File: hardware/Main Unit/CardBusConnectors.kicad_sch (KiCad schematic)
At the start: 5 parts, among them J2 61801525123, J3 61801525123, U3 SN74CB3Q3257PWR

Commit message: Finish 3.3V regulator
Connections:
- net V_SUPPLY renamed V_{SUPPLY}
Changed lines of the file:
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@@
 		)
 	)
-	(label "V_SUPPLY"
+	(label "V_{SUPPLY}"
 		(at 200.66 115.57 0)
 		(effects
@@
 		)
 	)
-	(label "V_SUPPLY"
+	(label "V_{SUPPLY}"
 		(at 203.2 48.26 0)
 		(effects
@@
 		)
 	)
-	(hierarchical_label "V_SUPPLY"
+	(hierarchical_label "V_{SUPPLY}"
 		(shape input)
 		(at 200.66 48.26 180)

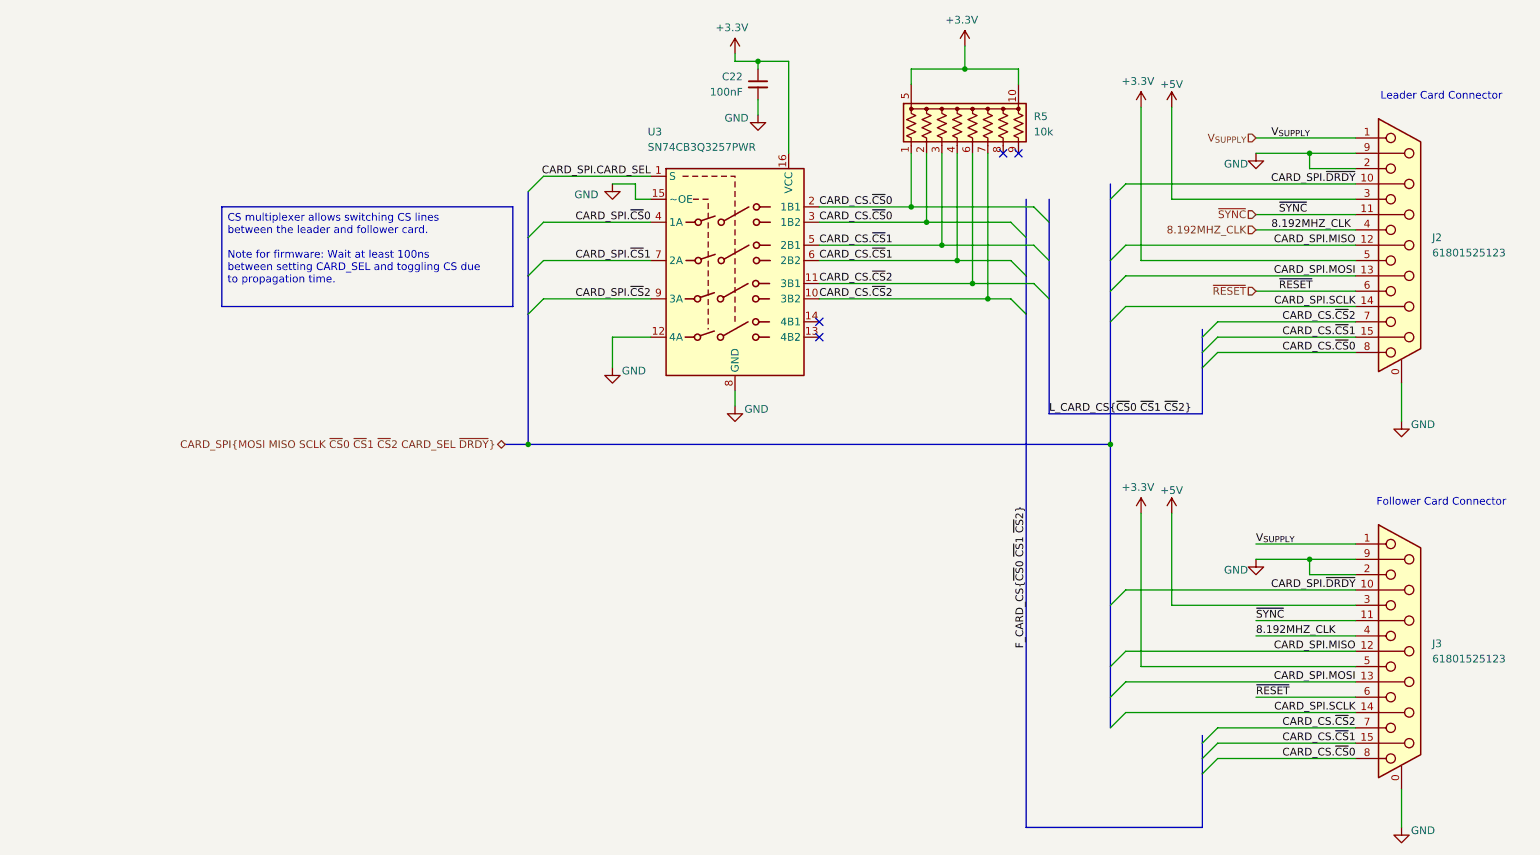
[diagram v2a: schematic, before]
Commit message: Main unit: Add USB port for MCU and 3.3VA rail, start on routing
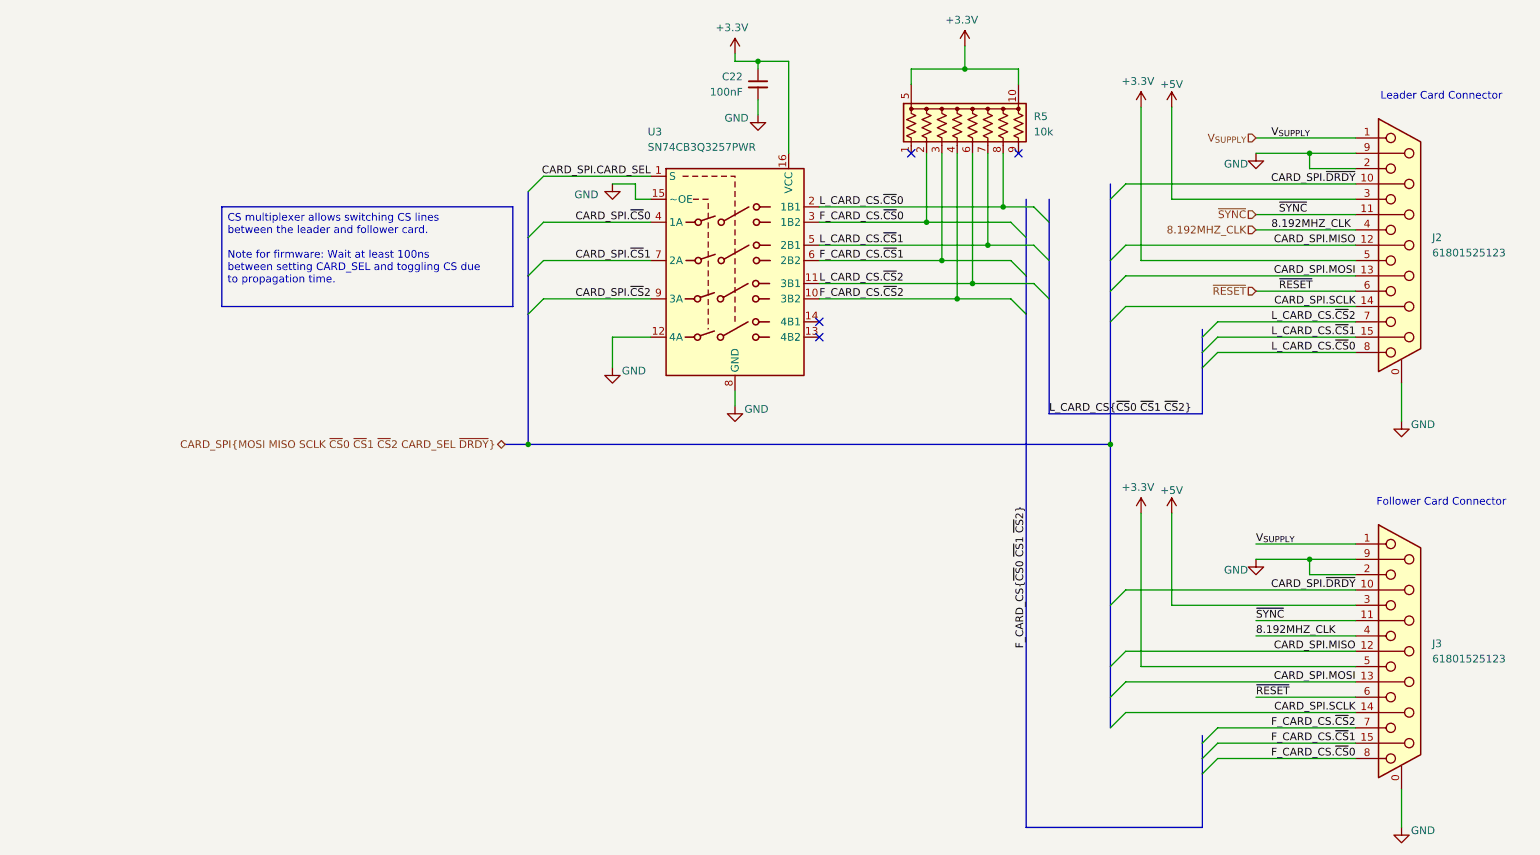
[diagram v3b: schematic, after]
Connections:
- net L_CARD_CS.~{CS}0: now reaches R5.8 (R7)
- net L_CARD_CS.~{CS}0: now also J2.8, U3.2 (1B1)
- net CARD_CS.~{CS}0 renamed F_CARD_CS.~{CS}0
- net F_CARD_CS.~{CS}0: no longer J2.8, R5.1 (R1), U3.2 (1B1)
- net CARD_CS.~{CS}1 renamed F_CARD_CS.~{CS}1
- net F_CARD_CS.~{CS}1: no longer J2.15 (P15), R5.4 (R4), U3.5 (2B1)
- net CARD_CS.~{CS}2 renamed L_CARD_CS.~{CS}2
- net L_CARD_CS.~{CS}2: no longer J3.7, R5.7 (R6), U3.10 (3B2)
- new net F_CARD_CS.~{CS}2: J3.7, R5.4 (R4), U3.10 (3B2)
- new net L_CARD_CS.~{CS}1: J2.15 (P15), R5.7 (R6), U3.5 (2B1)

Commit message: Geographical reannotate
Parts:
- renumbered C22 to C36, J3 to J6, J2 to J7, R5 to R12, U3 to U6
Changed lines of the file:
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@@
 		(dnp no)
 		(fields_autoplaced yes)
-		(property "Reference" "J3"
+		(property "Reference" "J6"
 			(at 229.87 132.0799 0)
 			(effects
@@
 			(project "HackerDAQ Main Unit"
 				(path "/7d91f165-331a-4c48-9d02-ee2a0aa7e94a/647fa122-ba55-4257-82a5-33756e3f8461"
-					(reference "J3")
-					(unit 1)
-				)
-				(path "/7d91f165-331a-4c48-9d02-ee2a0aa7e94a/65abad2d-a04a-4486-8762-5ae3bd8749b5"
-					(reference "J9")
-					(unit 1)
-				)
-				(path "/7d91f165-331a-4c48-9d02-ee2a0aa7e94a/9f275358-f91d-4a0c-a7c6-dd286f9a4cb9"
-					(reference "J7")
-					(unit 1)
-				)
-				(path "/7d91f165-331a-4c48-9d02-ee2a0aa7e94a/a26c9c83-f4f8-48b6-a052-d2759c00eb1e"
-					(reference "J5")
+					(reference "J6")
+					(unit 1)
+				)
+				(path "/7d91f165-331a-4c48-9d02-ee2a0aa7e94a/65abad2d-a04a-4486-8762-5ae3bd8749b5"
+					(reference "J2")
+					(unit 1)
+				)
+				(path "/7d91f165-331a-4c48-9d02-ee2a0aa7e94a/9f275358-f91d-4a0c-a7c6-dd286f9a4cb9"
+					(reference "J4")
+					(unit 1)
+				)
+				(path "/7d91f165-331a-4c48-9d02-ee2a0aa7e94a/a26c9c83-f4f8-48b6-a052-d2759c00eb1e"
+					(reference "J8")
 					(unit 1)
 				)
@@
 		(dnp no)
 		(fields_autoplaced yes)
-		(property "Reference" "J2"
+		(property "Reference" "J7"
 			(at 229.87 64.7699 0)
 			(effects
@@
 			(project "HackerDAQ Main Unit"
 				(path "/7d91f165-331a-4c48-9d02-ee2a0aa7e94a/647fa122-ba55-4257-82a5-33756e3f8461"
-					(reference "J2")
-					(unit 1)
-				)
-				(path "/7d91f165-331a-4c48-9d02-ee2a0aa7e94a/65abad2d-a04a-4486-8762-5ae3bd8749b5"
-					(reference "J8")
-					(unit 1)
-				)
-				(path "/7d91f165-331a-4c48-9d02-ee2a0aa7e94a/9f275358-f91d-4a0c-a7c6-dd286f9a4cb9"
-					(reference "J6")
-					(unit 1)
-				)
-				(path "/7d91f165-331a-4c48-9d02-ee2a0aa7e94a/a26c9c83-f4f8-48b6-a052-d2759c00eb1e"
-					(reference "J4")
+					(reference "J7")
+					(unit 1)
+				)
+				(path "/7d91f165-331a-4c48-9d02-ee2a0aa7e94a/65abad2d-a04a-4486-8762-5ae3bd8749b5"
+					(reference "J3")
+					(unit 1)
+				)
+				(path "/7d91f165-331a-4c48-9d02-ee2a0aa7e94a/9f275358-f91d-4a0c-a7c6-dd286f9a4cb9"
+					(reference "J5")
+					(unit 1)
+				)
+				(path "/7d91f165-331a-4c48-9d02-ee2a0aa7e94a/a26c9c83-f4f8-48b6-a052-d2759c00eb1e"
+					(reference "J9")
 					(unit 1)
 				)
@@
 		(dnp no)
 		(fields_autoplaced yes)
-		(property "Reference" "R5"
+		(property "Reference" "R12"
 			(at 163.83 44.7039 0)
 			(effects
@@
 			(project "HackerDAQ Main Unit"
 				(path "/7d91f165-331a-4c48-9d02-ee2a0aa7e94a/647fa122-ba55-4257-82a5-33756e3f8461"
-					(reference "R5")
-					(unit 1)
-				)
-				(path "/7d91f165-331a-4c48-9d02-ee2a0aa7e94a/65abad2d-a04a-4486-8762-5ae3bd8749b5"
-					(reference "R8")
-					(unit 1)
-				)
-				(path "/7d91f165-331a-4c48-9d02-ee2a0aa7e94a/9f275358-f91d-4a0c-a7c6-dd286f9a4cb9"
-					(reference "R7")
-					(unit 1)
-				)
-				(path "/7d91f165-331a-4c48-9d02-ee2a0aa7e94a/a26c9c83-f4f8-48b6-a052-d2759c00eb1e"
-					(reference "R6")
+					(reference "R12")
+					(unit 1)
+				)
+				(path "/7d91f165-331a-4c48-9d02-ee2a0aa7e94a/65abad2d-a04a-4486-8762-5ae3bd8749b5"
+					(reference "R11")
+					(unit 1)
+				)
+				(path "/7d91f165-331a-4c48-9d02-ee2a0aa7e94a/9f275358-f91d-4a0c-a7c6-dd286f9a4cb9"
+					(reference "R13")
+					(unit 1)
+				)
+				(path "/7d91f165-331a-4c48-9d02-ee2a0aa7e94a/a26c9c83-f4f8-48b6-a052-d2759c00eb1e"
+					(reference "R10")
 					(unit 1)
 				)
@@
 		(on_board yes)
 		(dnp no)
-		(property "Reference" "U3"
+		(property "Reference" "U6"
 			(at 99.822 47.244 0)
 			(effects
@@
 			(project "HackerDAQ Main Unit"
 				(path "/7d91f165-331a-4c48-9d02-ee2a0aa7e94a/647fa122-ba55-4257-82a5-33756e3f8461"
+					(reference "U6")
+					(unit 1)
+				)
+				(path "/7d91f165-331a-4c48-9d02-ee2a0aa7e94a/65abad2d-a04a-4486-8762-5ae3bd8749b5"
+					(reference "U7")
+					(unit 1)
+				)
+				(path "/7d91f165-331a-4c48-9d02-ee2a0aa7e94a/9f275358-f91d-4a0c-a7c6-dd286f9a4cb9"
+					(reference "U1")
+					(unit 1)
+				)
+				(path "/7d91f165-331a-4c48-9d02-ee2a0aa7e94a/a26c9c83-f4f8-48b6-a052-d2759c00eb1e"
 					(reference "U3")
-					(unit 1)
-				)
-				(path "/7d91f165-331a-4c48-9d02-ee2a0aa7e94a/65abad2d-a04a-4486-8762-5ae3bd8749b5"
-					(reference "U6")
-					(unit 1)
-				)
-				(path "/7d91f165-331a-4c48-9d02-ee2a0aa7e94a/9f275358-f91d-4a0c-a7c6-dd286f9a4cb9"
-					(reference "U5")
-					(unit 1)
-				)
-				(path "/7d91f165-331a-4c48-9d02-ee2a0aa7e94a/a26c9c83-f4f8-48b6-a052-d2759c00eb1e"
-					(reference "U4")
 					(unit 1)
 				)
@@
 		(on_board yes)
 		(dnp no)
-		(property "Reference" "C22"
+		(property "Reference" "C36"
 			(at 115.57 38.1062 0)
 			(effects
@@
 			(project "HackerDAQ Main Unit"
 				(path "/7d91f165-331a-4c48-9d02-ee2a0aa7e94a/647fa122-ba55-4257-82a5-33756e3f8461"
-					(reference "C22")
-					(unit 1)
-				)
-				(path "/7d91f165-331a-4c48-9d02-ee2a0aa7e94a/65abad2d-a04a-4486-8762-5ae3bd8749b5"
-					(reference "C26")
-					(unit 1)
-				)
-				(path "/7d91f165-331a-4c48-9d02-ee2a0aa7e94a/9f275358-f91d-4a0c-a7c6-dd286f9a4cb9"
-					(reference "C25")
-					(unit 1)
-				)
-				(path "/7d91f165-331a-4c48-9d02-ee2a0aa7e94a/a26c9c83-f4f8-48b6-a052-d2759c00eb1e"
-					(reference "C23")
-					(unit 1)
-				)
+					(reference "C36")
+					(unit 1)
+				)
+				(path "/7d91f165-331a-4c48-9d02-ee2a0aa7e94a/65abad2d-a04a-4486-8762-5ae3bd8749b5"
+					(reference "C28")
+					(unit 1)
+				)
+				(path "/7d91f165-331a-4c48-9d02-ee2a0aa7e94a/9f275358-f91d-4a0c-a7c6-dd286f9a4cb9"
+					(reference "C1")
+					(unit 1)
+				)
+				(path "/7d91f165-331a-4c48-9d02-ee2a0aa7e94a/a26c9c83-f4f8-48b6-a052-d2759c00eb1e"
+					(reference "C2")
+					(unit 1)
+				)
